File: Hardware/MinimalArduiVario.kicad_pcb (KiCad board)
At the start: 2 copper layers, 30 x 36 mm, 34 parts, among them IC1 ATMEGA328P-A, J1 test AMP, J2 CONN_01X08, Q1 DMC2038LVT, SW1 Select, SW2 Up, SW3 Down, SW4 on/off

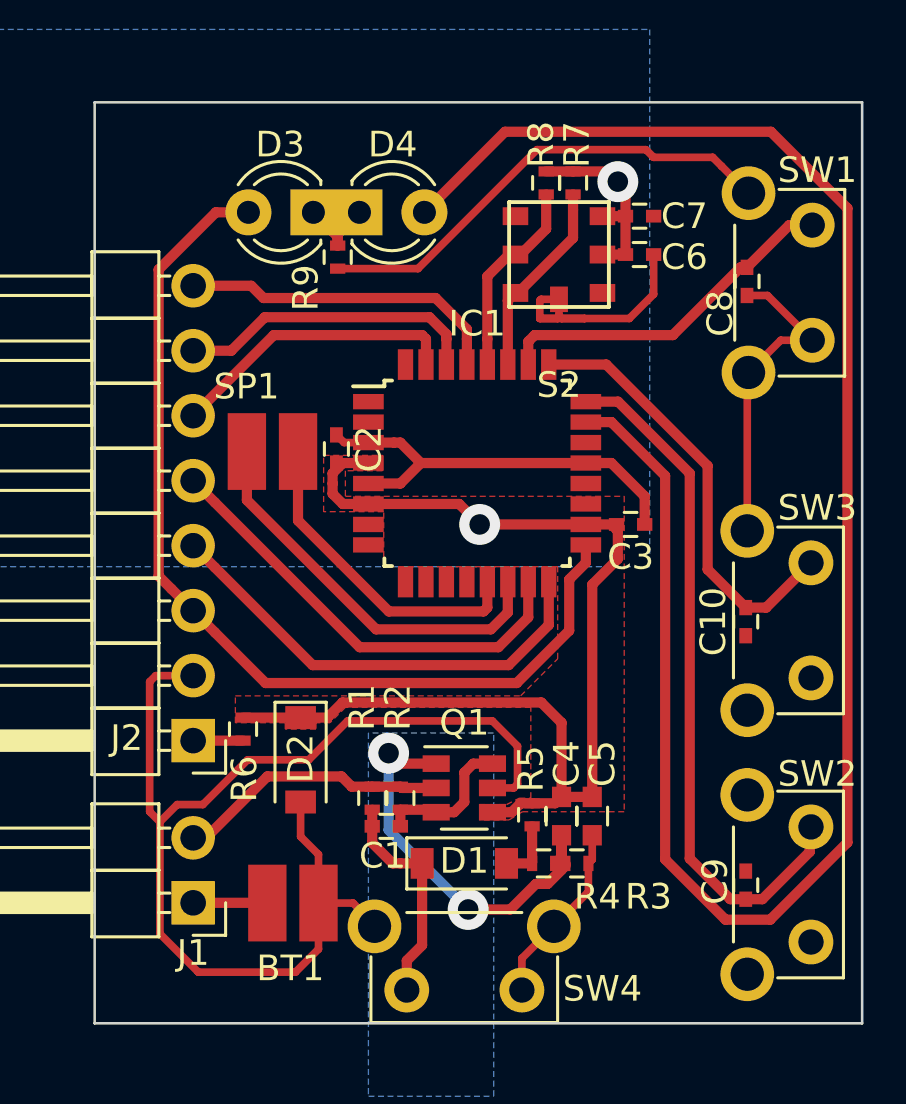
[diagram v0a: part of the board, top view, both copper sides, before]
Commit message: Prepare dev software
Change Adafruit lib for BMP180 and test all peripherals. Set fuses into "extra_script.py".
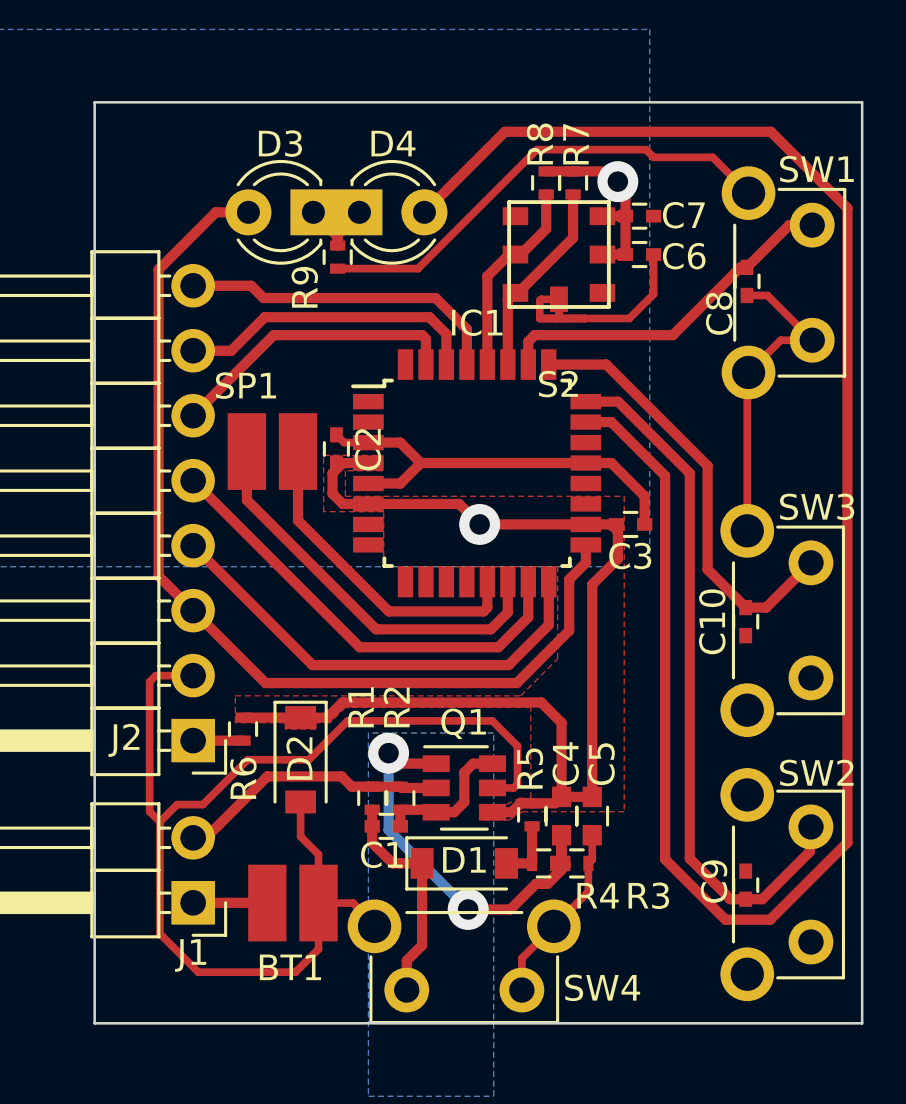
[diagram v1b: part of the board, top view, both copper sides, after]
